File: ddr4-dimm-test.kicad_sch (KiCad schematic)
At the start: 150 parts

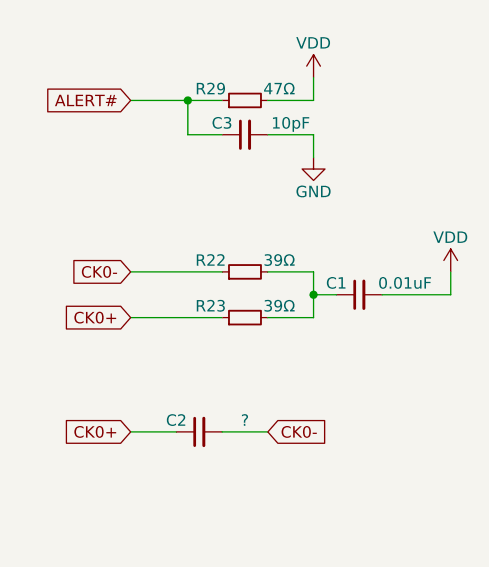
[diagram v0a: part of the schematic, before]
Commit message: change cap value
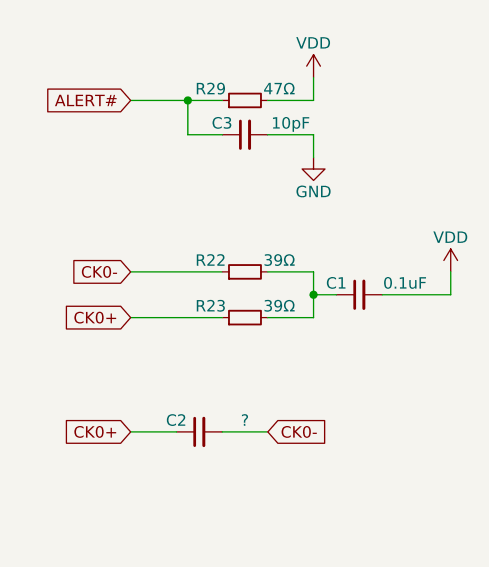
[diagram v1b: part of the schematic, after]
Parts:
- C1: value 0.01uF -> 0.1uF
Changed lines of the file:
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@@
 			)
 		)
-		(property "Value" "0.01uF"
+		(property "Value" "0.1uF"
 			(at 568.96 347.98 90)
 			(effects
